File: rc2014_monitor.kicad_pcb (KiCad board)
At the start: 2 copper layers, 99.1 x 49.9 mm, 33 parts, among them J1 RC2014Pro, J3 USB_B_Micro, SW1 SW_Coded_Octal-8, U1 74HCT138, U2 74HCT151, U3 74HCT244, U4 74HCT244, U5 74HCT244, U6 74HCT32, U7 MAX40200AUK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

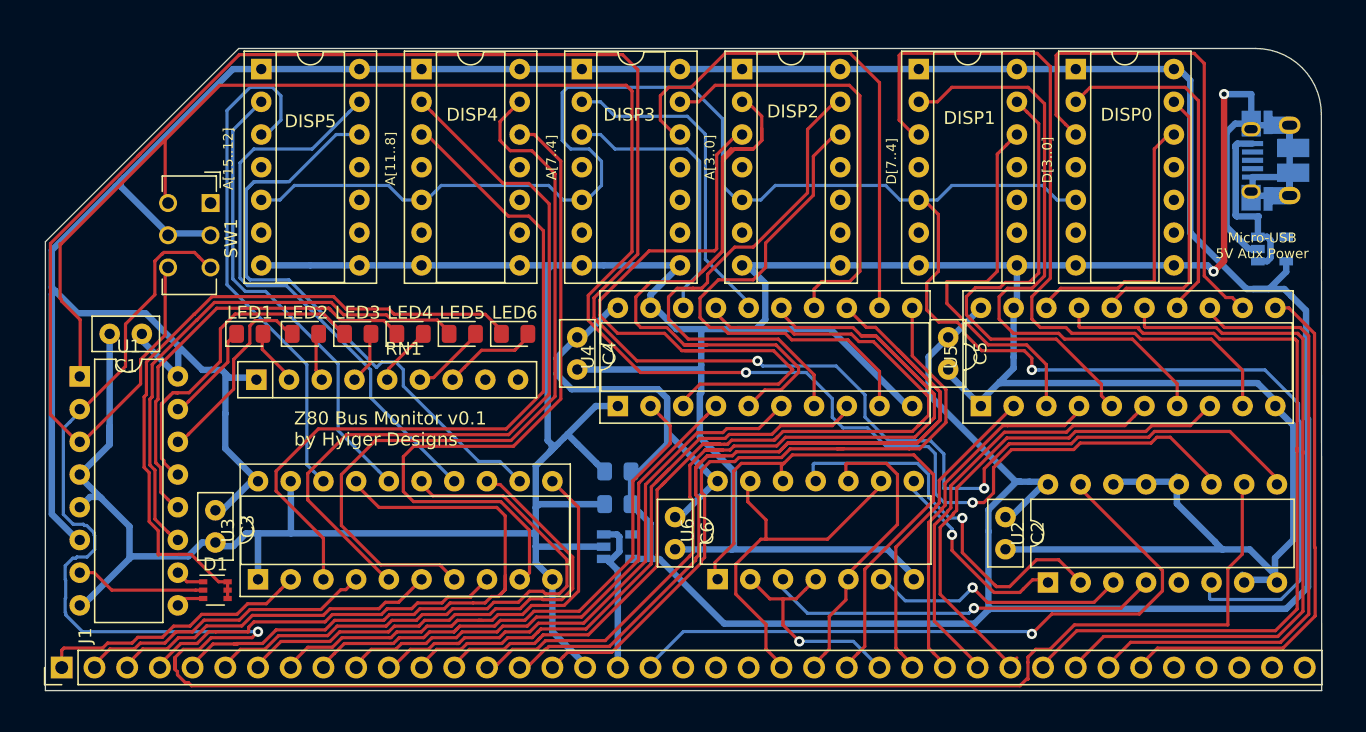
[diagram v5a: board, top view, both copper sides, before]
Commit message: added pro bus, generated gerbers
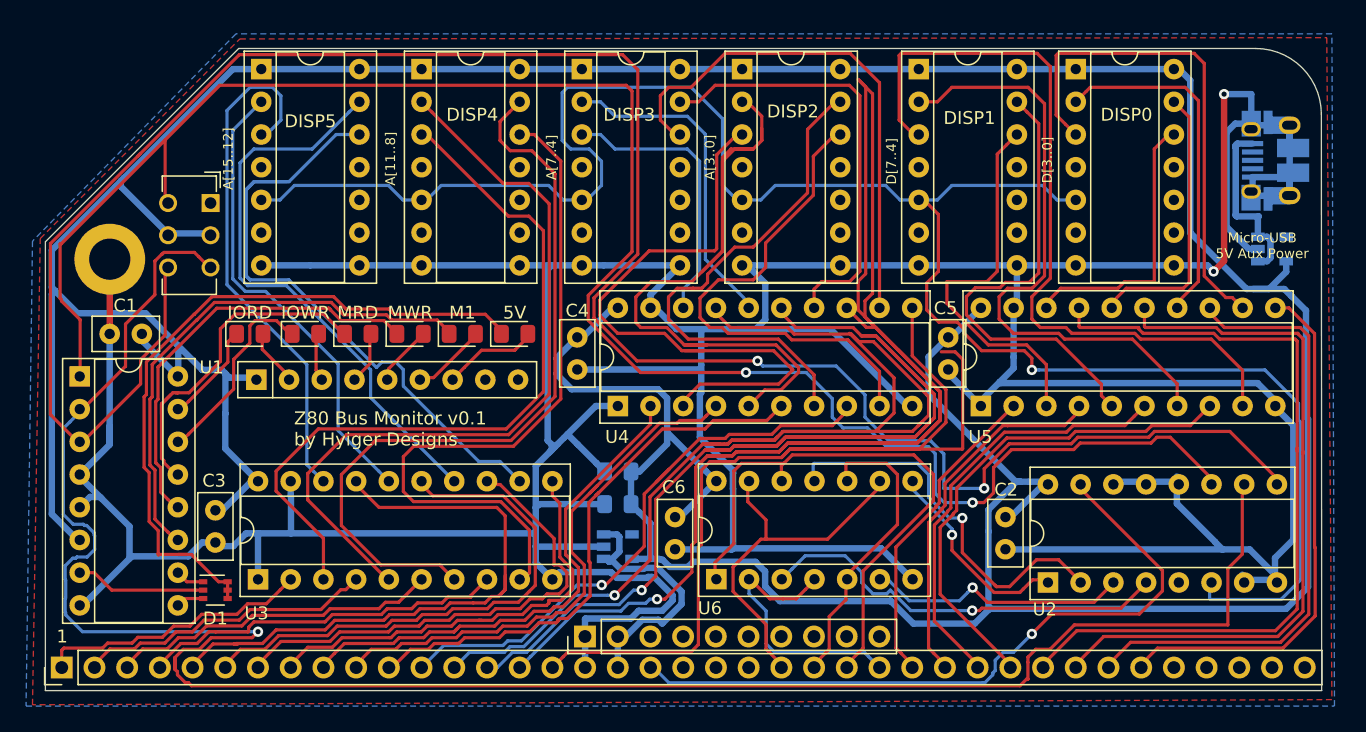
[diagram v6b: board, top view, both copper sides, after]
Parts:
- added J2: Pro Bus, Connector_PinHeader_2.54mm:PinHeader_1x10_P2.54mm_Vertical, F.Cu at (118.1, 123.1)
- added J4: Conn_01x01_Female, MountingHole:MountingHole_3.2mm_M3_ISO14580_Pad, F.Cu at (81.2, 93.8)
- J1: value RC2014Pro -> Z80 Bus
- U1, U2: footprint Package_DIP:DIP-16_W7.62mm -> Package_DIP:DIP-16_W7.62mm_Socket
- U6: footprint Package_DIP:DIP-14_W7.62mm -> Package_DIP:DIP-14_W7.62mm_Socket
- moved U6 0.10 mm to (128.3, 118.6)
- renumbered LED6 to 5V, LED1 to IORD, LED2 to IOWR, LED5 to M1, LED3 to MRD, LED4 to MWR
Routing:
- net A1: track 82.4 -> 146.7 mm, vias 0 -> 1
- net A2: track 72.5 -> 108.1 mm, vias 0 -> 1
- net A0: track 53.3 -> 79.9 mm
- net A3: track 73.1 -> 96.1 mm, vias 0 -> 1
- net GND: track 418.5 -> 438.7 mm
- net 5V: track 12.3 -> 20.3 mm
- net ~IORQ: track 17.2 -> 21.5 mm, vias 1 -> 0
- net A10: track 45.0 -> 41.2 mm
- net A6: track 39.7 -> 42.1 mm
- net IO_RD: track 30.8 -> 32.6 mm
- net ~M1: track 53.4 -> 55.0 mm
- net A7: track 42.4 -> 41.0 mm
- net A5: track 42.5 -> 43.7 mm
- net +5V: track 349.7 -> 350.7 mm
- net A4: track 46.4 -> 45.6 mm, vias 0 -> 1
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- added copper zone on B.Cu, net GND
- added copper zone on F.Cu, net GND
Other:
- board text added: "1"

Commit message: Added reset circuit
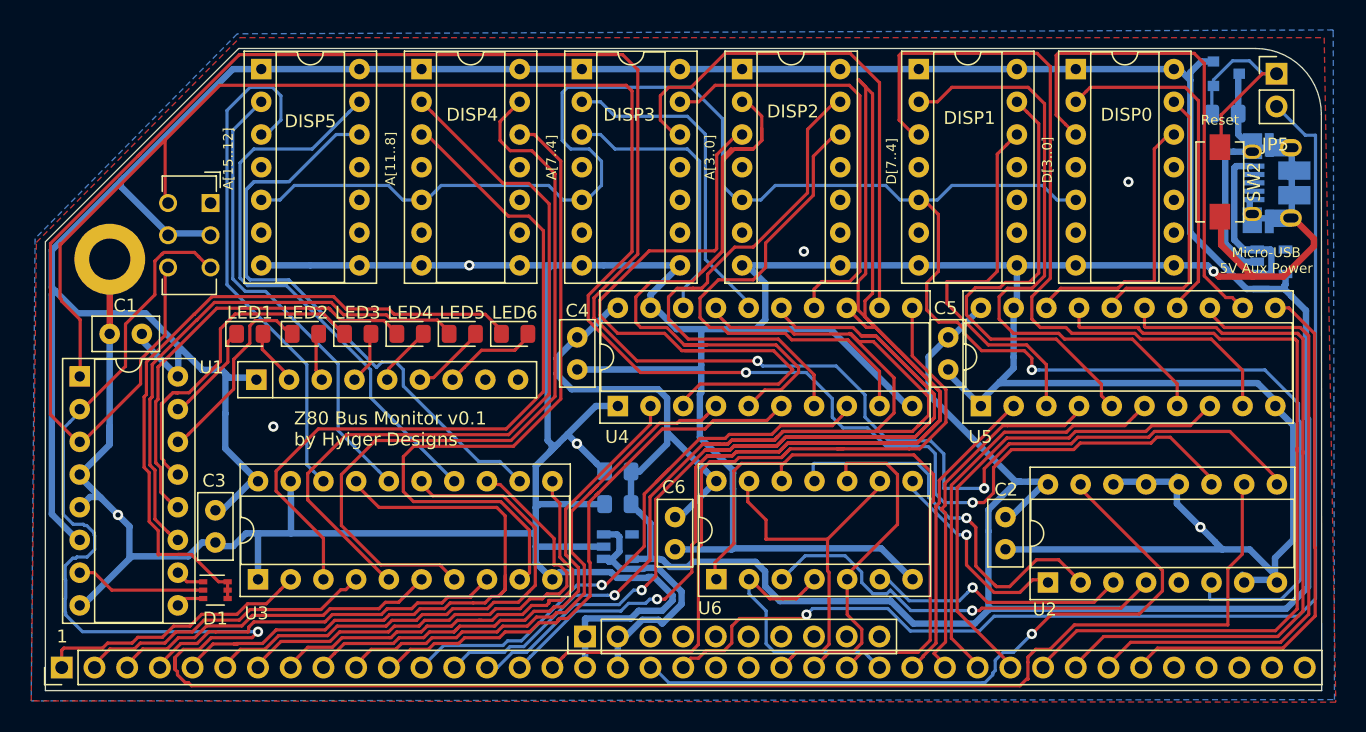
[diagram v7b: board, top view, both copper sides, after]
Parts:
- added C9: 100nF, Capacitor_SMD:C_0805_2012Metric_Pad1.15x1.40mm_HandSolder, B.Cu at (167.8, 82.5)
- added JP5: Jumper_2_Open, Connector_PinHeader_2.54mm:PinHeader_1x02_P2.54mm_Vertical, F.Cu at (171.8, 79.4)
- added SW2: SW_Push, Button_Switch_SMD:SW_SPST_EVQPE1, F.Cu at (167.4, 87.8)
- added U9: DS1813R-5+T&R, Package_TO_SOT_SMD:SOT-23, B.Cu at (167.9, 79.4)
- moved J3 1.75 mm to (171.8, 87.9)
- moved U7 0.99 mm to (171.4, 94.0)
- renumbered IORD to LED1, IOWR to LED2, MRD to LED3, MWR to LED4, M1 to LED5, 5V to LED6
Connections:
- J1 pad 20: (no net) -> ~RESET
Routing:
- net ~RESET: track 0.00 -> 93.5 mm, vias 0 -> 1
- net A0: track 79.9 -> 57.6 mm
- net Net-(C9-Pad1): track 0.00 -> 16.7 mm
- net Net-(J3-Pad1): track 19.3 -> 13.1 mm
- net ~RD: track 44.8 -> 47.6 mm
- net ~WR: track 23.3 -> 25.3 mm
- net +5V: track 350.7 -> 352.0 mm
- net D2: track 33.4 -> 32.3 mm
- net D3: track 38.8 -> 37.7 mm
- net D0: track 24.8 -> 24.0 mm
- net GND: track 438.7 -> 438.8 mm, vias 2 -> 8
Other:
- board text added: "Reset"

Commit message: label updates
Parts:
- J4: value Conn_01x01_Female -> M3 Mounting Hole
- JP5: value Jumper_2_Open -> Reset Enable
- SW1: value SW_Coded_Octal-8 -> Line Selection
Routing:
- net Net-(D1-Pad4): track 54.9 -> 54.4 mm
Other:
- board text added: "5V"
- board text added: "5V Aux"
- board text added: "IORD"
- board text added: "IOWR"
- board text added: "M1"
- board text added: "MRD"
- board text added: "MWR"
- board text removed: "Micro-USB 5V Aux Power"
